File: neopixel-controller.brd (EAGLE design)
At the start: 59 x 25.5 mm, 26 parts, among them Q1 BSS138, Q2 BSS138, U1 ESP-WROOM-02, U2 AP2112K

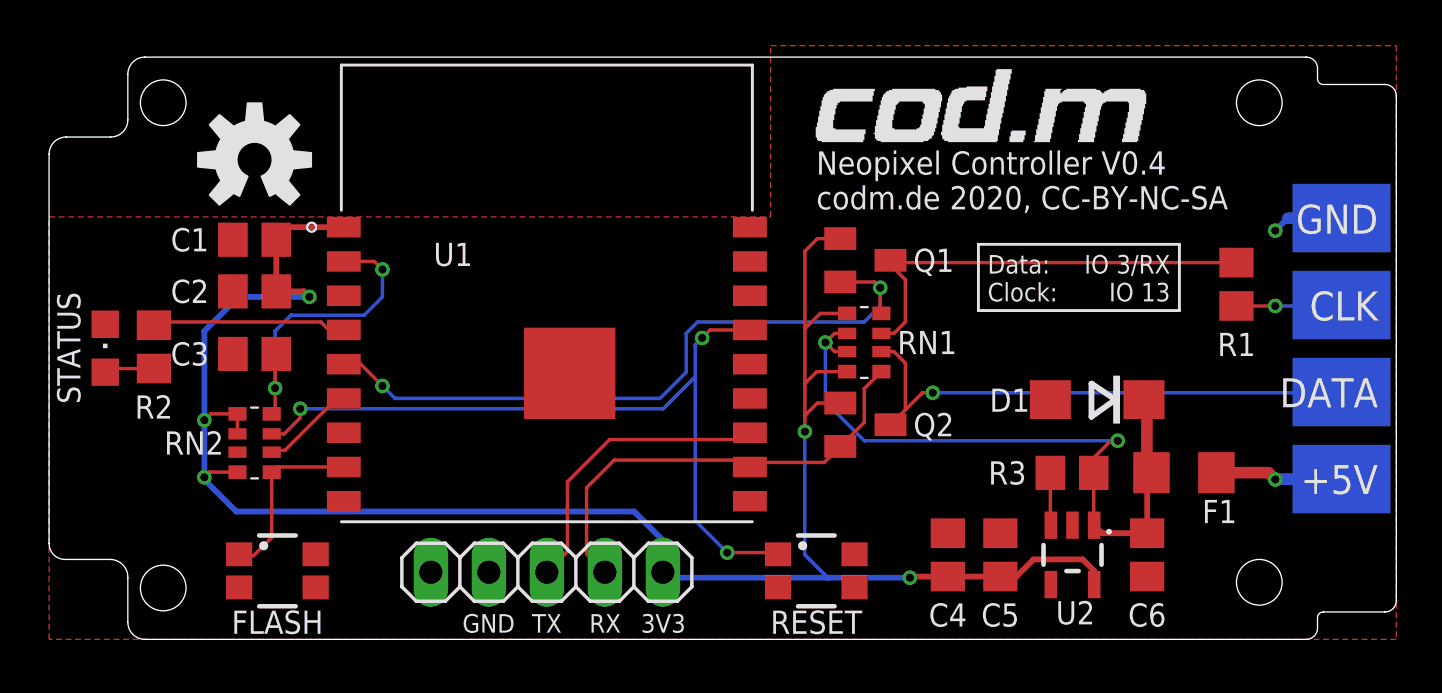
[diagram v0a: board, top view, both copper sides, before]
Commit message: added 74ahct125, rework for v0.5
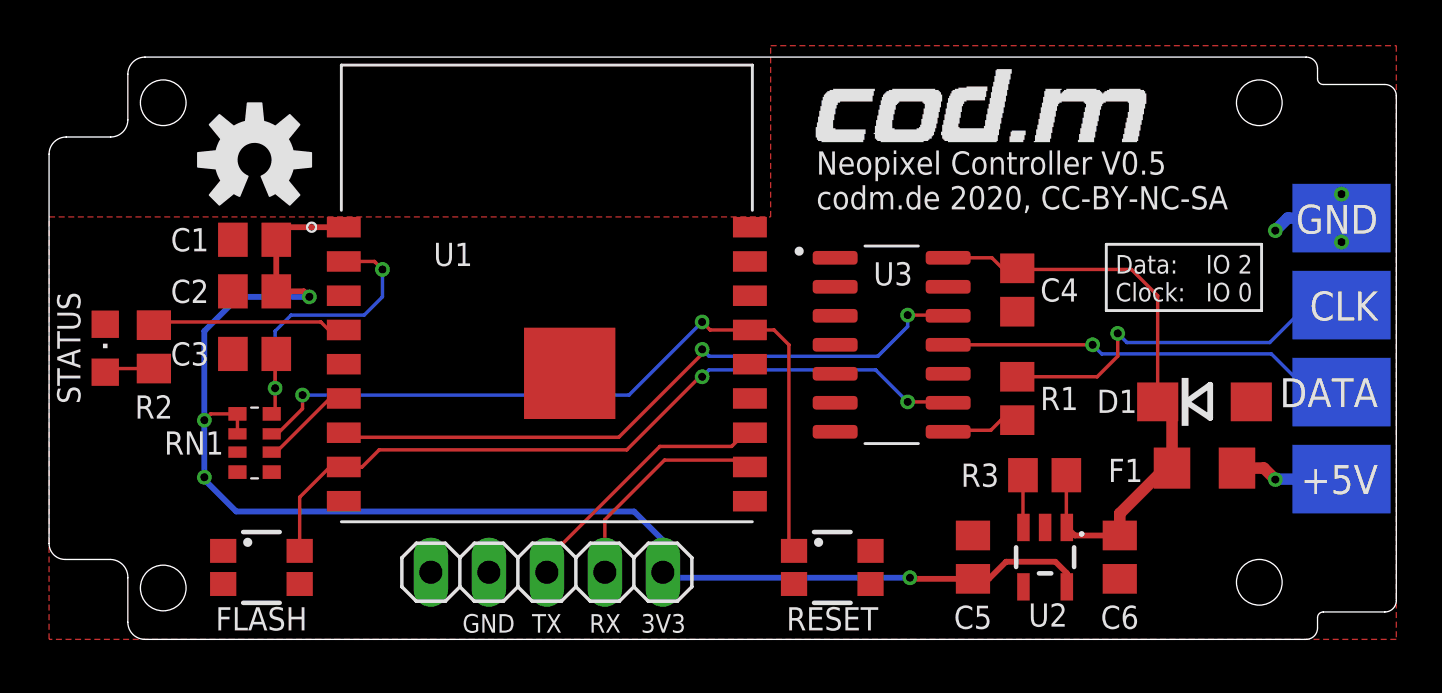
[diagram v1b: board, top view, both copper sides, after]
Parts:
- removed Q1, Q2: BSS138, adafruit:SOT23
- removed RN2: 10k, resistor-dil:EXB38V
- added U3: SN74AHCT125D, SN74AHCT125D:SOIC127P600X175-14N
- C4: value 1µ -> 100n
- C5, C6: value 10µ -> 1u
- R1: value 300 -> 470
- moved RN1 27.1 mm to (9.00, 8.60)
- moved C4 12.0 mm to (42.4, 15.3), turned to 90 degrees
- moved R1 10.8 mm to (42.4, 10.6), turned to 270 degrees
- moved D1 4.70 mm to (50.6, 10.4), turned to 0 degrees
- moved C6 1.20 mm to (46.9, 3.60)
- moved U2 1.20 mm to (43.6, 3.60)
- moved C5 1.20 mm to (40.5, 3.60)
- moved R3 1.20 mm to (43.6, 7.19)
- moved F1 0.92 mm to (50.6, 7.50)
- moved FLASH 0.72 mm to (9.30, 3.15)
- moved RESET 0.72 mm to (34.3, 3.15)
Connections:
- removed net FLASH: FLASH.1, RN2.1, U1.8
- new net DATA: U1.7, U3.12
- net +3V3: now also RN1.6; no longer C4.2, Q1.1, Q2.1, RN1.8, RN2.5, RN2.6, RN2.8
- net +5V: now also C4.2, U3.14; no longer RN1.6, RN1.7
- net BOOTMODE: now also RN1.2; no longer RN2.2
- net CHIPEN: now also RN1.4; no longer RN2.4
- net CLK: now also FLASH.3, U1.8, U3.9; no longer Q1.2, RN1.4, U1.5
- net CLK-5V: now also U3.8; no longer Q1.3, RN1.3
- net DATA-5V: now also U3.11; no longer Q2.3, RN1.2
- net GND: now also FLASH.4, RN1.7, U3.1, U3.4, U3.7; no longer FLASH.2, RN2.7
- net RST: now also RN1.3; no longer RN2.3
- net RXD: no longer Q2.2, RN1.1
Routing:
- net DATA: track 0.00 -> 29.4 mm, vias 0 -> 2
- net +3V3: track 87.9 -> 62.7 mm, vias 5 -> 4
- net CLK-5V: track 19.4 -> 3.24 mm
- net N$3: track 4.62 -> 16.4 mm
- net RXD: track 20.2 -> 9.86 mm
- net FLASH: track 7.87 -> 0.00 mm
- net DATA-5V: track 23.6 -> 18.1 mm
- net +5V: track 31.2 -> 26.8 mm, vias 2 -> 0
- net CLK: track 30.7 -> 33.7 mm
- net TXD: track 13.2 -> 11.8 mm
- net VCC: track 5.61 -> 4.79 mm
- net RST: track 34.4 -> 34.6 mm, vias 3 -> 2
- net GND: vias 1 -> 3
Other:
- board text added: "90060-0.5"
- board text added: "IO 2 IO 0"
- board text added: "Neopixel Controller V0.5 codm.de 2020, CC-BY-NC-SA"
- board text removed: "90060-0.4"
- board text removed: "IO 3/RX IO 13"
- board text removed: "Neopixel Controller V0.4 codm.de 2020, CC-BY-NC-SA"

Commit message: v0.5 pr
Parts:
- F1: value 16V 750mA -> 8V 500mA
- R1: value 470 -> 330
- moved R3 4.68 mm to (46.6, 3.60), turned to 270 degrees
- moved C6 2.21 mm to (49.1, 3.60)
- moved U$100 0.50 mm to (28.0, 9.50)
- moved U$102 0.50 mm to (34.0, 13.5)
- moved D1 0.50 mm to (50.2, 10.7)
- moved U3 0.41 mm to (37.0, 12.5)
- moved C4 0.40 mm to (42.4, 14.9)
- moved R1 0.40 mm to (42.4, 10.2), turned to 90 degrees
- moved U$2 0.40 mm to (9.00, 21.4)
- moved F1 0.30 mm to (50.3, 7.50)
- moved C5 0.16 mm to (40.3, 3.60), turned to 90 degrees
- moved U2 0.16 mm to (43.5, 3.50), turned to 0 degrees
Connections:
- removed net N$3: R1.1, U$101.P$2
- new net DATA-5VR: R1.1, U$101.P$3
- net CLK-5V: now also U$101.P$2; no longer R1.2
- net DATA-5V: now also R1.2; no longer U$101.P$3
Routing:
- net CLK-5V: track 3.24 -> 23.1 mm, vias 0 -> 1
- net N$3: track 16.4 -> 0.00 mm, vias 1 -> 0
- net DATA-5VR: track 0.00 -> 16.3 mm, vias 0 -> 1
- net DATA-5V: track 18.1 -> 4.03 mm, vias 1 -> 0
- net +3V3: track 62.7 -> 60.9 mm, vias 4 -> 3
- net RST: track 34.6 -> 35.9 mm
- net CLK: track 33.7 -> 32.4 mm
- net GND: track 3.13 -> 2.10 mm, vias 3 -> 2
- net +5V: track 26.8 -> 27.8 mm
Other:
- board text added: "CC-BY-SA"
- board text added: "Wi-Fi Pixel Controller V0.5 codm.de 2020, CC-BY-SA"
- board text added: "codm.de, 2020"
- board text removed: "CC-BY-NC-SA"
- board text removed: "Neopixel Controller V0.5 codm.de 2020, CC-BY-NC-SA"
